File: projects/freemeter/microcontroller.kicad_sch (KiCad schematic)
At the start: 12 parts, among them J401 CONN_02X03, U401 ATMEGA16M1, U402 MCP2561-E_SN, Y401 Crystal_SMD

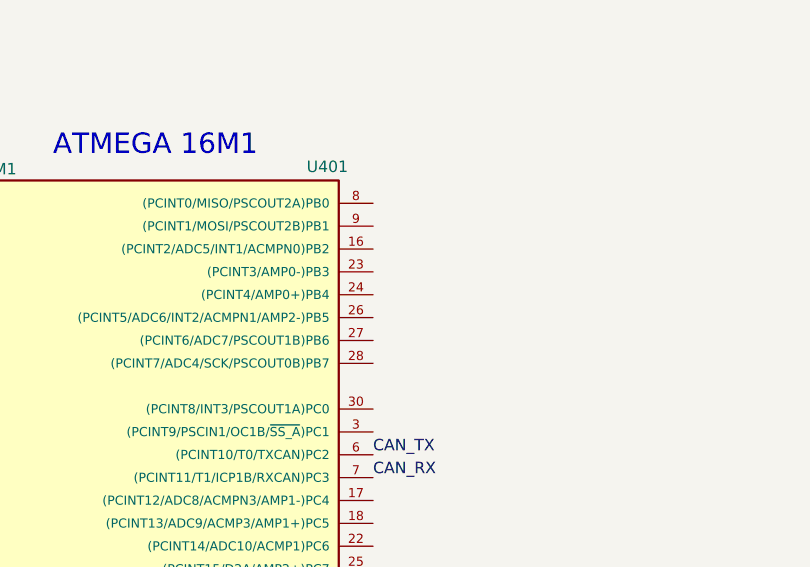
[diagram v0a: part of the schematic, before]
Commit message: Made modifications to adc, microcontroller and flyback converter schematics
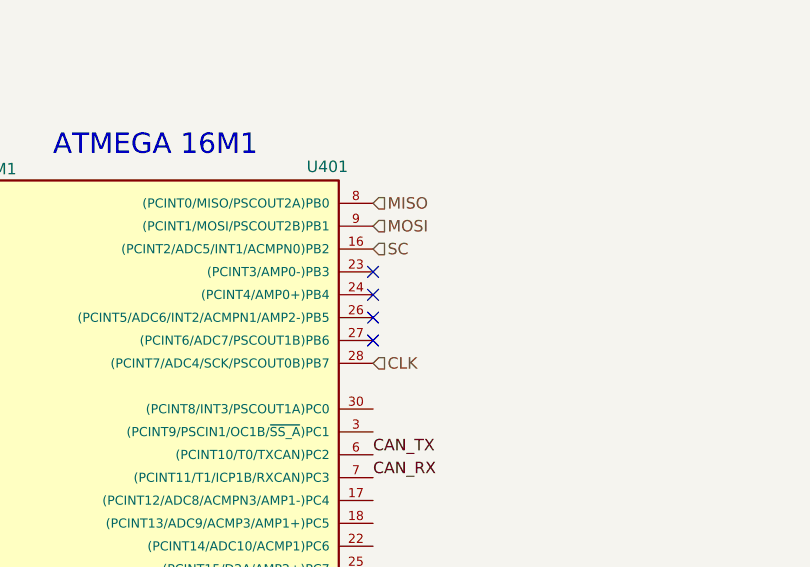
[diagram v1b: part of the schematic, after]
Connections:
- net MISO: now also U401.8 ((PCINT0/MISO/PSCOUT2A)PB0)
- net MOSI: now also U401.9 ((PCINT1/MOSI/PSCOUT2B)PB1)
- net SC: now reaches U401.16 ((PCINT2/ADC5/INT1/ACMPN0)PB2)
- net CLK: now reaches U401.28 ((PCINT7/ADC4/SCK/PSCOUT0B)PB7)
- no-connect marks 2 -> 6
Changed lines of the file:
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@@
   (junction (at 252.73 171.45) (diameter 0) (color 0 0 0 0)
   )
+  (no_connect (at 236.22 102.87))
+  (no_connect (at 236.22 105.41))
+  (no_connect (at 236.22 100.33))
   (no_connect (at 388.62 52.07))
+  (no_connect (at 236.22 107.95))
   (no_connect (at 180.34 110.49))
   (wire (pts (xy 176.53 156.21) (xy 180.34 156.21))
@@
     (effects (font (size 1.27 1.27)) (justify right bottom))
   )
+  (hierarchical_label "CLK" (shape input) (at 236.22 110.49 0)
+    (effects (font (size 1.27 1.27)) (justify left))
+  )
+  (hierarchical_label "MOSI" (shape input) (at 236.22 95.25 0)
+    (effects (font (size 1.27 1.27)) (justify left))
+  )
+  (hierarchical_label "MISO" (shape input) (at 236.22 92.71 0)
+    (effects (font (size 1.27 1.27)) (justify left))
+  )
+  (hierarchical_label "SC" (shape input) (at 236.22 97.79 0)
+    (effects (font (size 1.27 1.27)) (justify left))
+  )
   (symbol (lib_id "power:GND") (at 392.43 218.44 0) (unit 1)

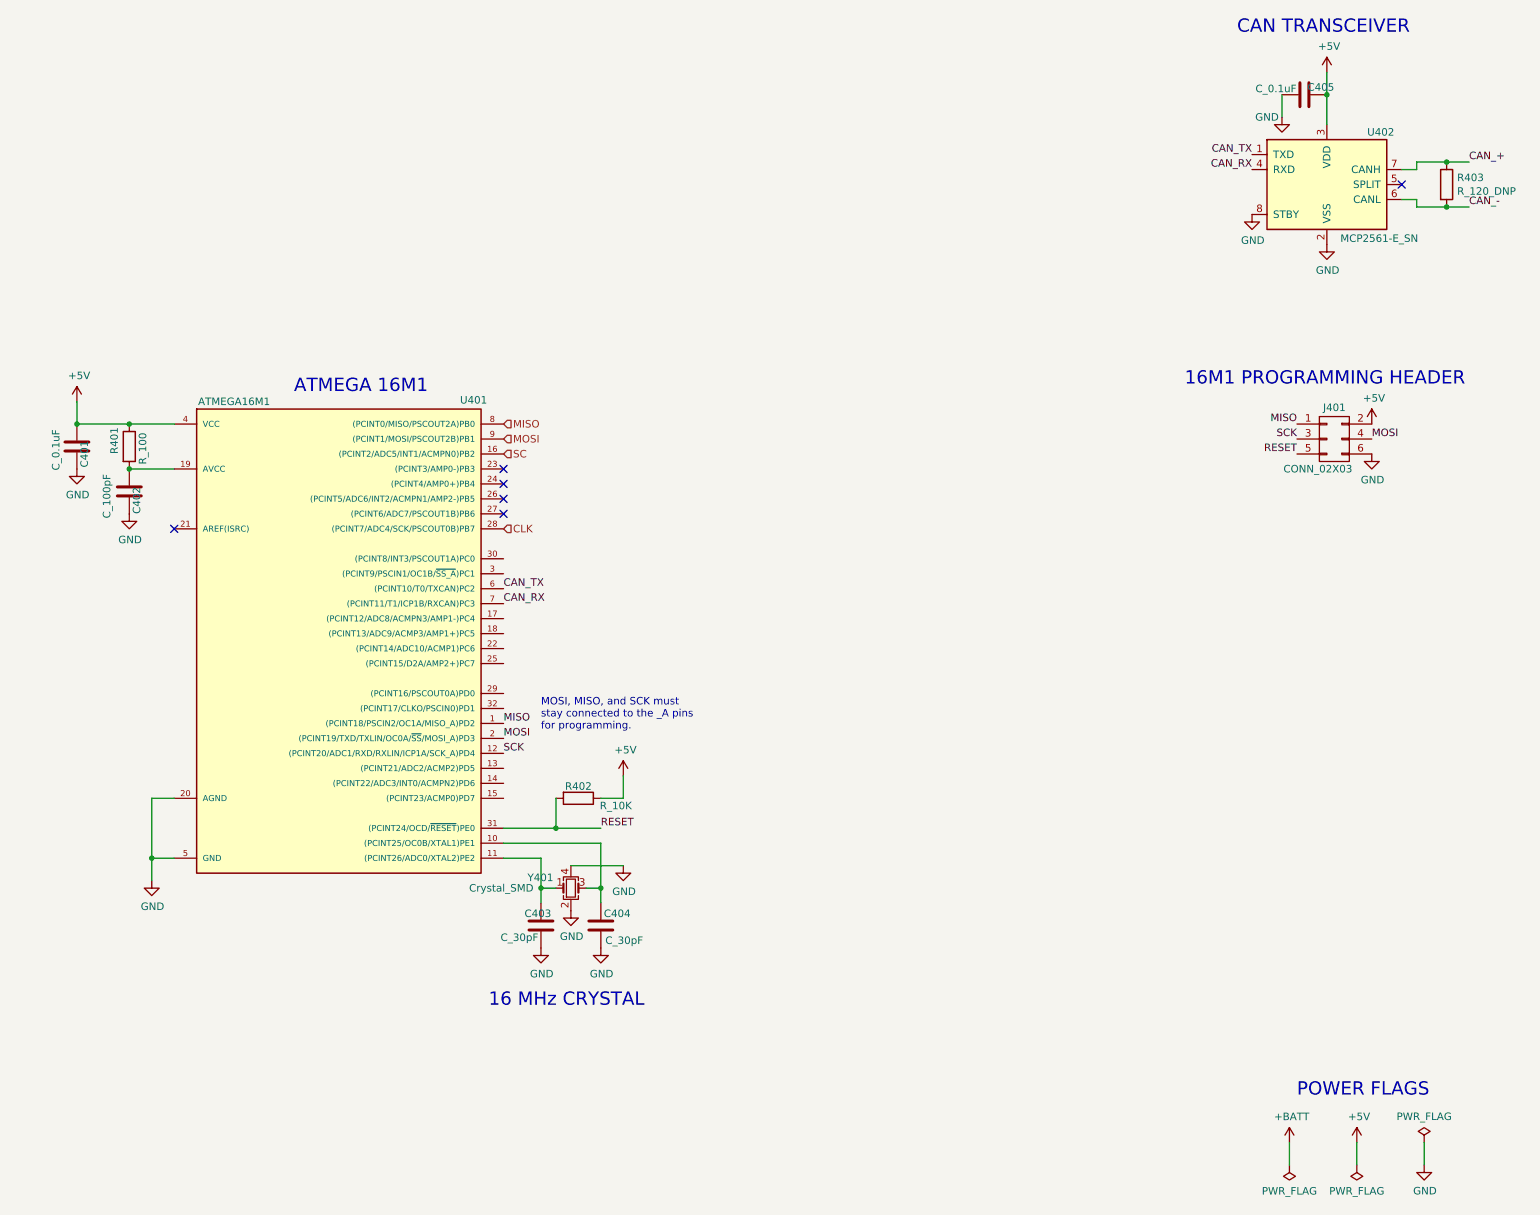
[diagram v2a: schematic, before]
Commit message: Adding changes to the freemeter schematic added LDO, renamed GND to GND1 and GND2, created global variables for +5V supply for HV and LV, added SLK,  cleaned up the schematic
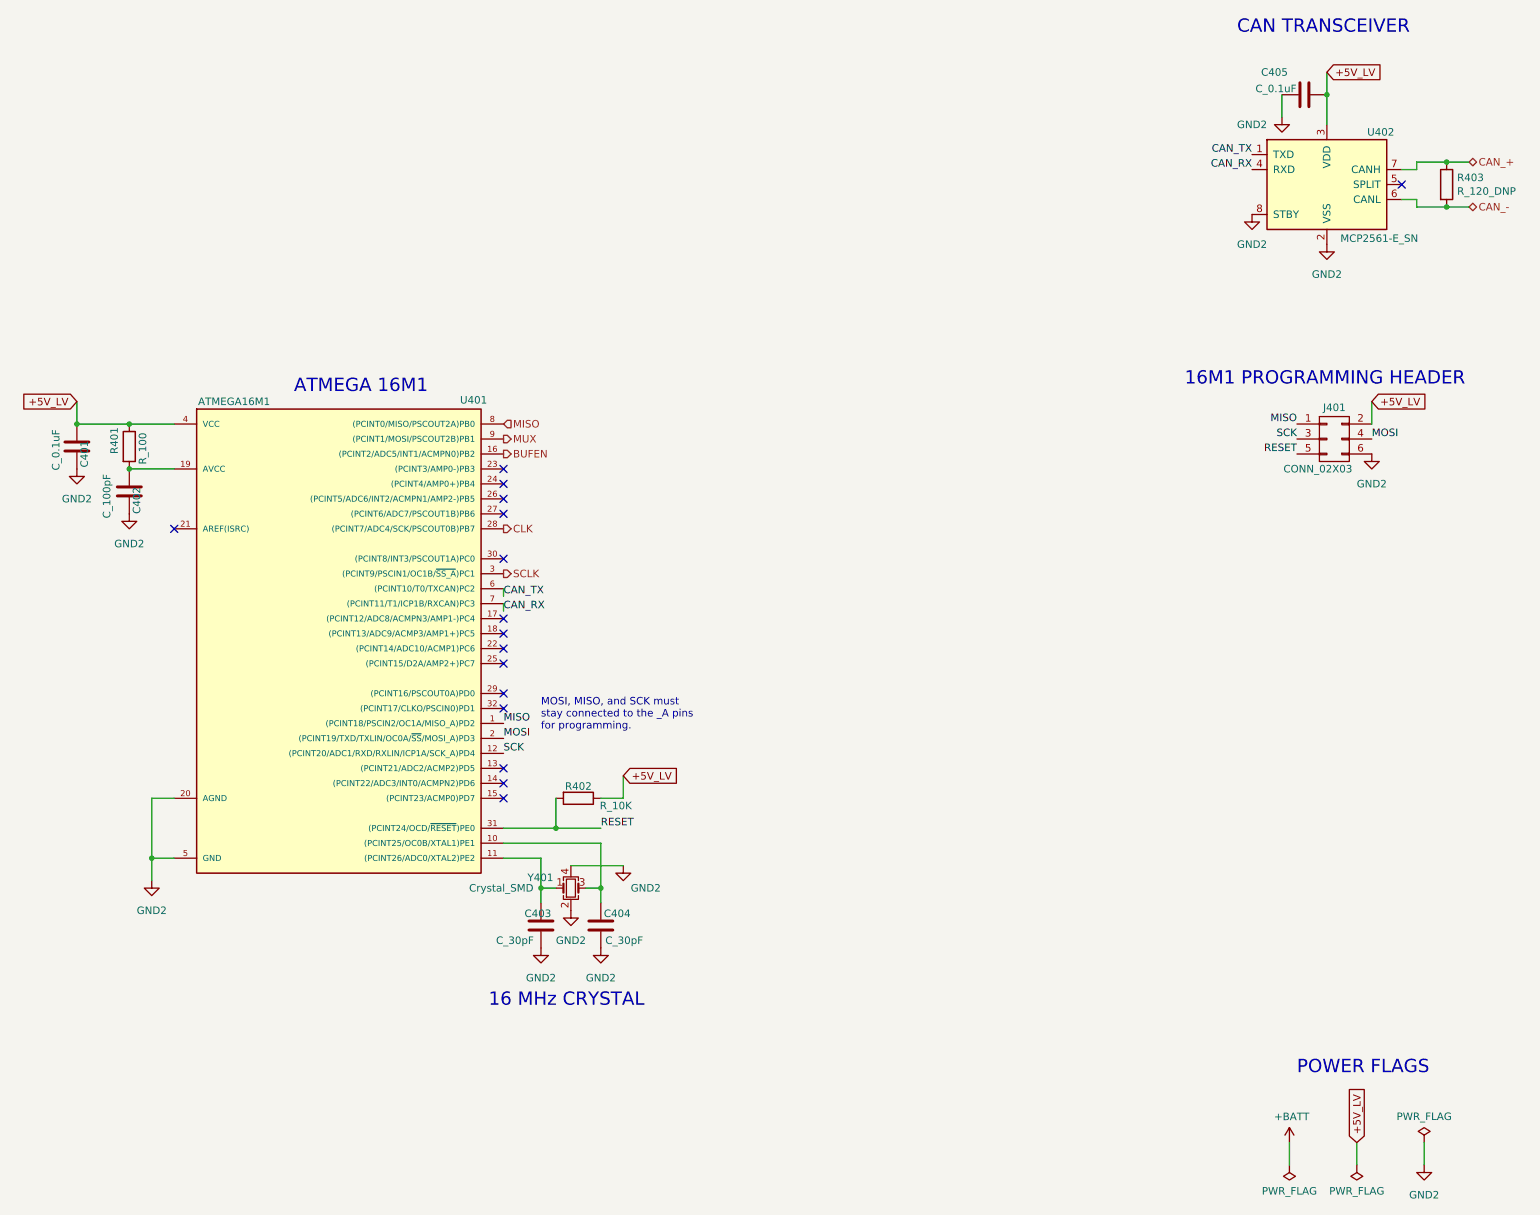
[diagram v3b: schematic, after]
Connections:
- net MOSI: no longer U401.9 ((PCINT1/MOSI/PSCOUT2B)PB1)
- net SCLK : now reaches U401.3 ((PCINT9/PSCIN1/OC1B/~{SS_A})PC1)
- net +5V renamed +5V_LV
- net GND renamed GND2
- net SC renamed BUFEN
- new net MUX: U401.9 ((PCINT1/MOSI/PSCOUT2B)PB1)
- no-connect marks 6 -> 16

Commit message: Final Changes to Freemeter
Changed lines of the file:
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@@
     (effects (font (size 1.27 1.27)) (justify right bottom))
   )
-  (global_label "+5V_LV" (shape input) (at 381 214.63 90) (fields_autoplaced)
+  (global_label "+5V_LV" (shape output) (at 381 214.63 90) (fields_autoplaced)
     (effects (font (size 1.27 1.27)) (justify left))
-    (property "Intersheet References" "${INTERSHEET_REFS}" (id 0) (at 381.0794 205.2621 90)
+    (property "Intersheet References" "${INTERSHEET_REFS}" (id 0) (at 380.9206 205.2621 90)
       (effects (font (size 1.27 1.27)) (justify left) hide)
     )

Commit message: Updating + partial layout
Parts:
- added D401: LED_0805, footprints:LED_0805_OEM, symbol OEM:LED_0805
- added R404: R_1K, footprints:R_0805_OEM, symbol formula:R_1K
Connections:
- net GND2: now also D401.1 (K)
- net DEBUG_LED: now reaches U401.23 ((PCINT3/AMP0-)PB3)
- net DEBUG_LED: now also R404.1
- new net: D401.2 (A), R404.2
- no-connect marks 16 -> 15

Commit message: Updating PCB and Schematic after first layout
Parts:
- C401, C402, C403, C404, C405: footprint footprints:C_0805_OEM -> footprints:C_0603_1608Metric
- R401, R402, R403, R404: footprint footprints:R_0805_OEM -> footprints:R_0603_1608Metric
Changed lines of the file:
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@@
       (effects (font (size 1.27 1.27)) (justify left))
     )
-    (property "Footprint" "footprints:R_0805_OEM" (id 2) (at 152.4 92.71 0)
+    (property "Footprint" "footprints:R_0603_1608Metric" (id 2) (at 152.4 92.71 0)
       (effects (font (size 1.27 1.27)) hide)
     )
@@
       (effects (font (size 1.27 1.27)) (justify left))
     )
-    (property "Footprint" "footprints:C_0805_OEM" (id 2) (at 164.7952 100.33 0)
+    (property "Footprint" "footprints:C_0603_1608Metric" (id 2) (at 164.7952 100.33 0)
       (effects (font (size 1.27 1.27)) hide)
     )
@@
       (effects (font (size 1.27 1.27)) (justify left))
     )
-    (property "Footprint" "footprints:C_0805_OEM" (id 2) (at 173.6852 107.95 0)
+    (property "Footprint" "footprints:C_0603_1608Metric" (id 2) (at 173.6852 107.95 0)
       (effects (font (size 1.27 1.27)) hide)
     )
@@
       (effects (font (size 1.27 1.27)) (justify left))
     )
-    (property "Footprint" "footprints:C_0805_OEM" (id 2) (at 243.5352 181.61 0)
+    (property "Footprint" "footprints:C_0603_1608Metric" (id 2) (at 243.5352 181.61 0)
       (effects (font (size 1.27 1.27)) hide)
     )
@@
       (effects (font (size 1.27 1.27)) (justify left))
     )
-    (property "Footprint" "footprints:C_0805_OEM" (id 2) (at 253.6952 181.61 0)
+    (property "Footprint" "footprints:C_0603_1608Metric" (id 2) (at 253.6952 181.61 0)
       (effects (font (size 1.27 1.27)) hide)
     )
@@
     (property "Reference" "R402" (id 0) (at 248.92 154.178 90))
     (property "Value" "R_10K" (id 1) (at 255.27 157.48 90))
-    (property "Footprint" "footprints:R_0805_OEM" (id 2) (at 248.92 154.432 0)
+    (property "Footprint" "footprints:R_0603_1608Metric" (id 2) (at 248.92 154.432 0)
       (effects (font (size 1.27 1.27)) hide)
     )
@@
     (property "Reference" "C405" (id 0) (at 367.03 33.02 90))
     (property "Value" "C_0.1uF" (id 1) (at 367.284 35.814 90))
-    (property "Footprint" "footprints:C_0805_OEM" (id 2) (at 368.3 37.7952 0)
+    (property "Footprint" "footprints:C_0603_1608Metric" (id 2) (at 368.3 37.7952 0)
       (effects (font (size 1.27 1.27)) hide)
     )
@@
       (effects (font (size 1.27 1.27)) (justify left))
     )
-    (property "Footprint" "footprints:R_0805_OEM" (id 2) (at 365.76 48.26 0)
+    (property "Footprint" "footprints:R_0603_1608Metric" (id 2) (at 365.76 48.26 0)
       (effects (font (size 1.27 1.27)) (justify left) hide)
     )
@@
       (effects (font (size 1.27 1.27)) (justify left))
     )
-    (property "Footprint" "footprints:R_0805_OEM" (id 2) (at 319.532 46.99 0)
-      (effects (font (size 1.27 1.27)) hide)
-    )
+    (property "Footprint" "footprints:R_0603_1608Metric" (id 2) (at 319.532 46.99 0)
+      (effects (font (size 1.27 1.27)) hide)
+    )
